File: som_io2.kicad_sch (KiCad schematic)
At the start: 8 parts, among them J1 Hermaphroditic_Molex_203456-0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, Y1 Oscillator_156.25MHz_SG3225EEN

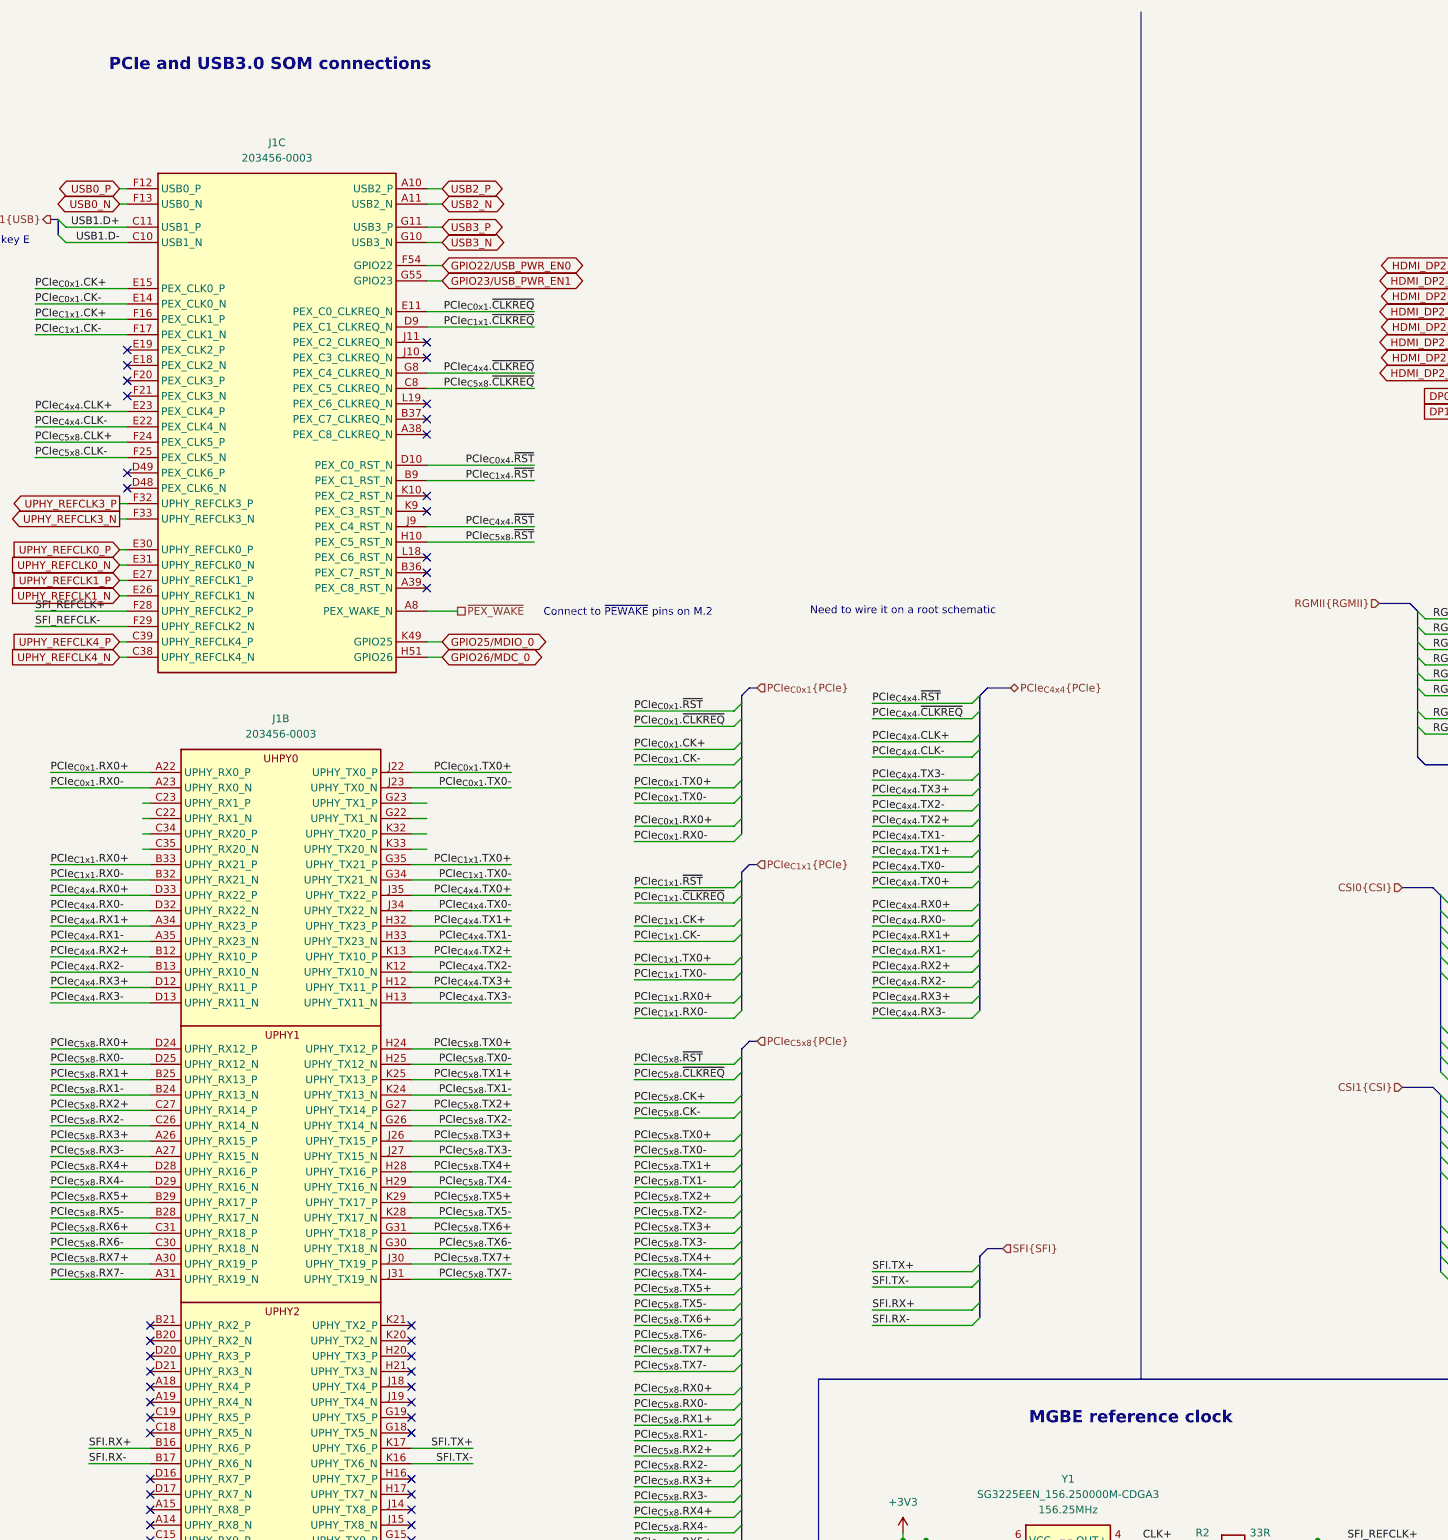
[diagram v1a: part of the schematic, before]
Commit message: [#82837] Standardise sheet sections text size
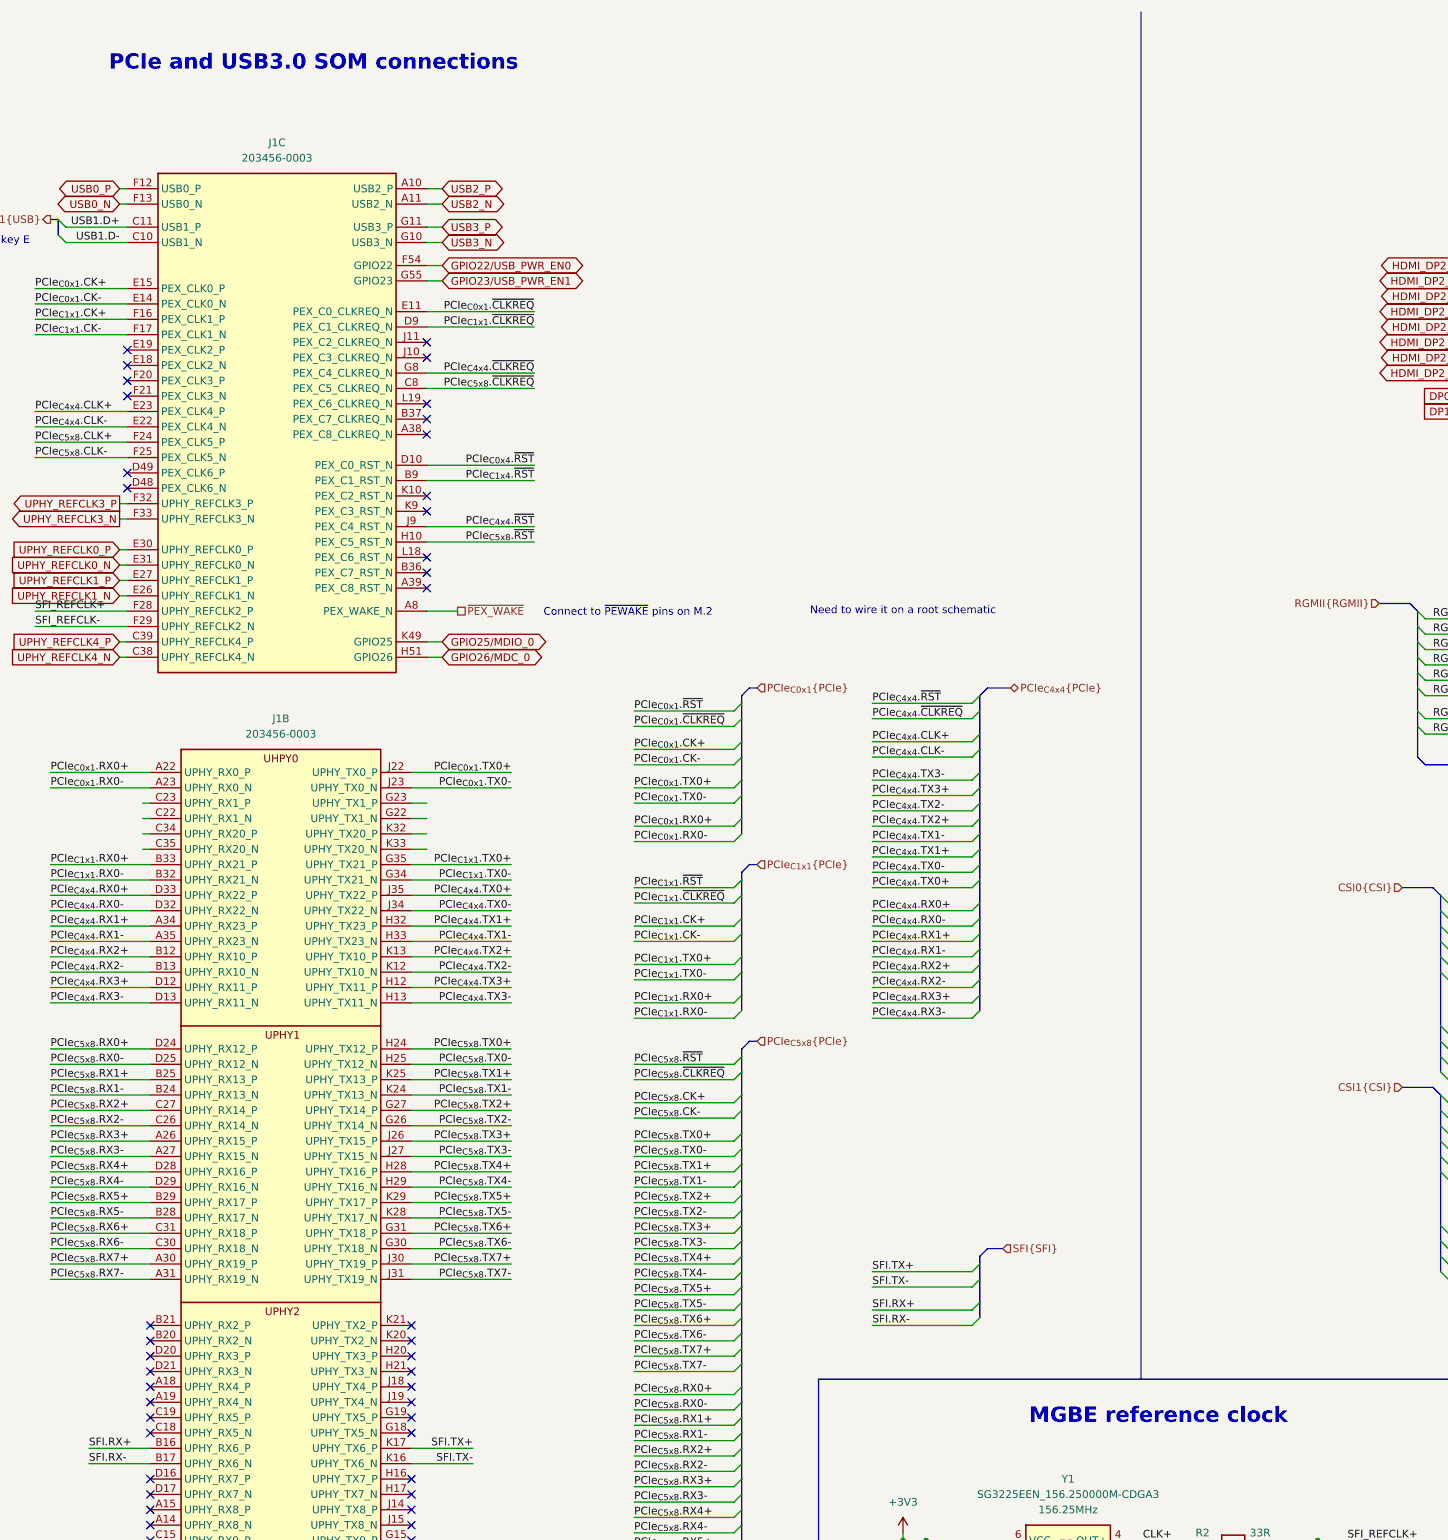
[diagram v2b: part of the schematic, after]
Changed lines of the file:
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@@
 		(effects
 			(font
-				(size 2 2)
+				(size 2.54 2.54)
 				(thickness 0.508)
 				(bold yes)
@@
 		(effects
 			(font
-				(size 2 2)
+				(size 2.54 2.54)
 				(thickness 0.508)
 				(bold yes)

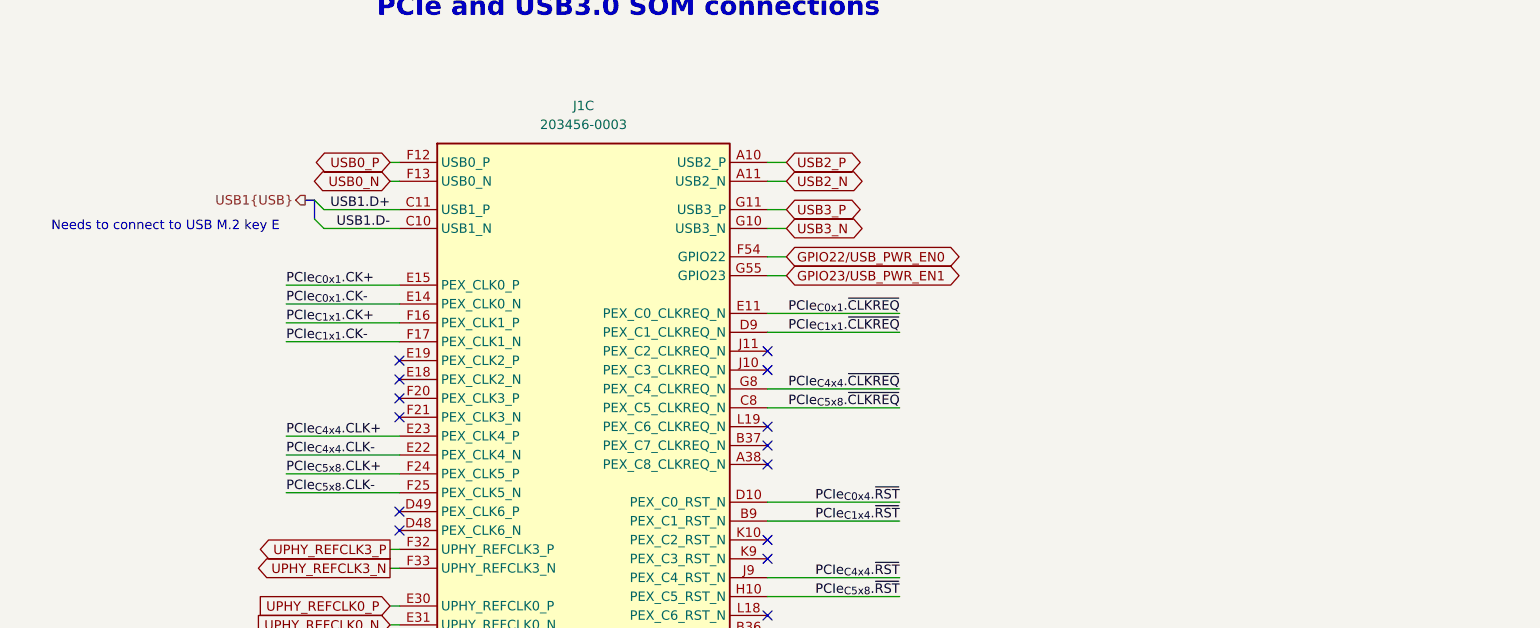
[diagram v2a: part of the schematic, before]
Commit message: [#82837] Reorganize project: split each USB subsheet into two subsheets
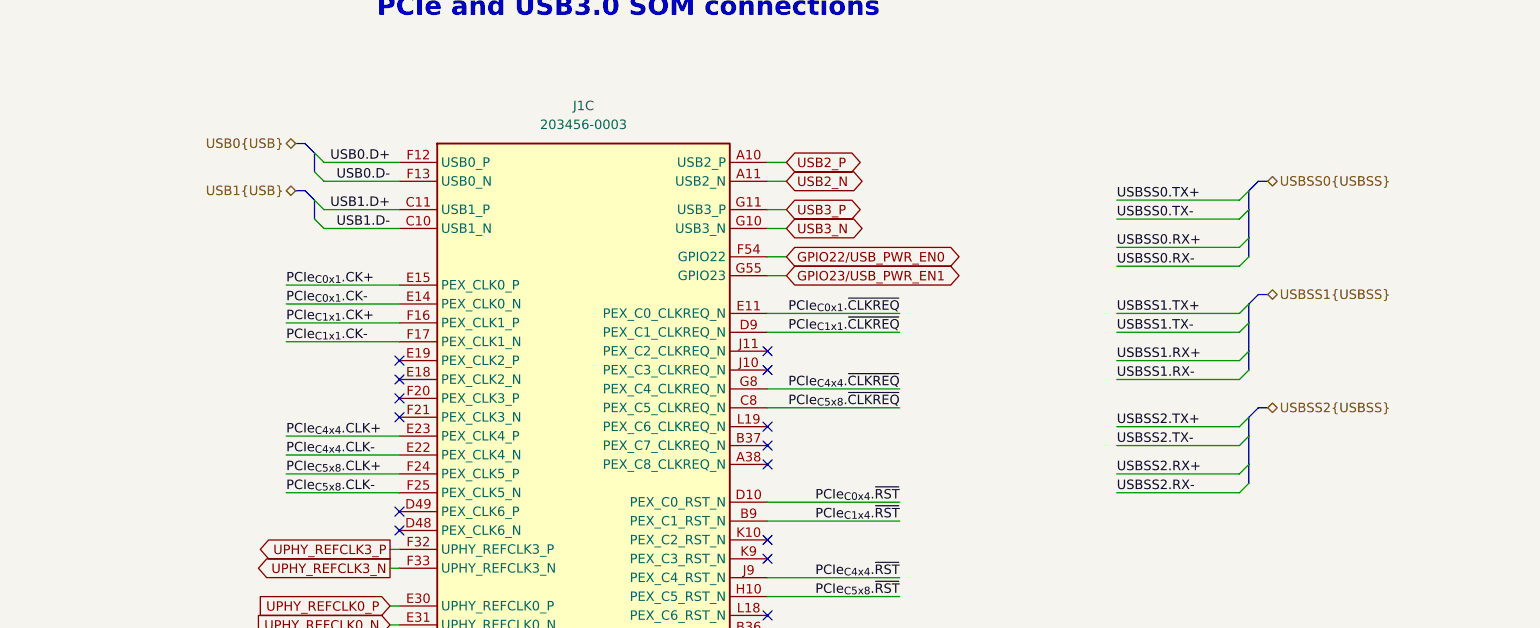
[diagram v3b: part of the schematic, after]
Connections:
- net USB0_N renamed USB0.D-
- net USB0_P renamed USB0.D+
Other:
- note removed: "Needs to connect to USB M.2 key E"

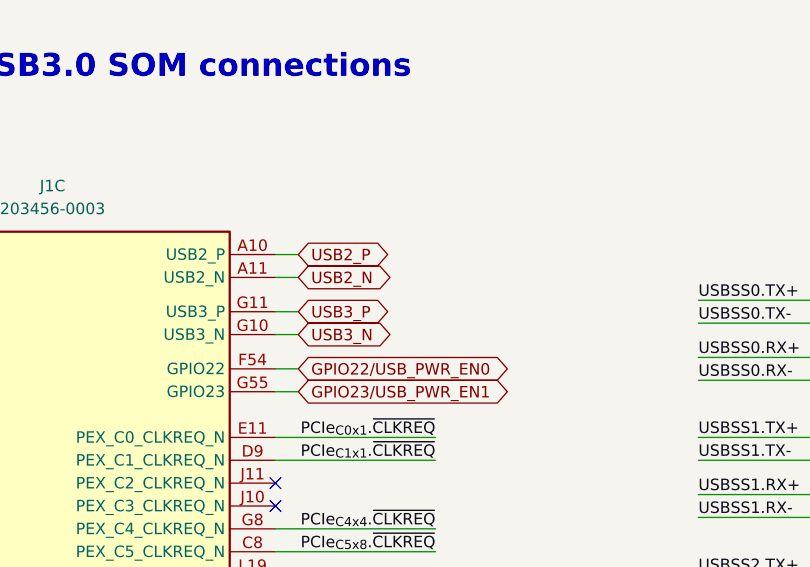
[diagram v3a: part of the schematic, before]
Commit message: [#82837] Cleanup USB Hub schematic and add vbus connections
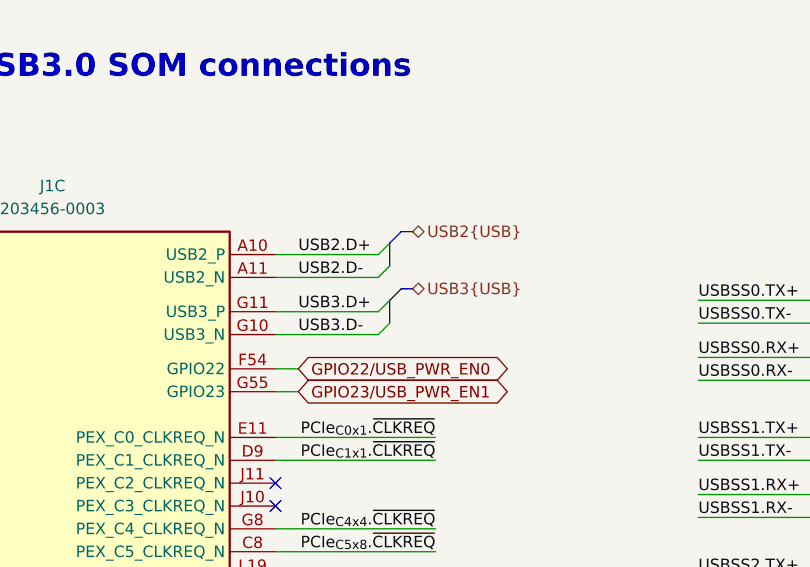
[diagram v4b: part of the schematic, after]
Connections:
- net USB2_N renamed USB2.D-
- net USB2_P renamed USB2.D+
- net USB3_N renamed USB3.D-
- net USB3_P renamed USB3.D+
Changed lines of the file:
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@@
 	)
 	(bus_entry
+		(at 138.43 49.53)
+		(size 1.27 -1.27)
+		(stroke
+			(width 0)
+			(type default)
+		)
+	)
+	(bus_entry
 		(at 179.07 163.83)
 		(size -1.27 1.27)
@@
 	)
 	(bus_entry
+		(at 138.43 43.18)
+		(size 1.27 -1.27)
+		(stroke
+			(width 0)
+			(type default)
+		)
+	)
+	(bus_entry
 		(at 179.07 193.04)
 		(size -1.27 1.27)
@@
 	)
 	(bus_entry
+		(at 138.43 46.99)
+		(size 1.27 -1.27)
+		(stroke
+			(width 0)
+			(type default)
+		)
+	)
+	(bus_entry
 		(at 191.77 83.82)
 		(size -1.27 1.27)
@@
 	)
 	(bus_entry
+		(at 138.43 40.64)
+		(size 1.27 -1.27)
+		(stroke
+			(width 0)
+			(type default)
+		)
+	)
+	(bus_entry
 		(at 179.07 196.85)
 		(size -1.27 1.27)
@@
 	(wire
 		(pts
-			(xy 129.54 40.64) (xy 127 40.64)
+			(xy 127 40.64) (xy 138.43 40.64)
 		)
 		(stroke
@@
 	(wire
 		(pts
-			(xy 129.54 46.99) (xy 127 46.99)
+			(xy 127 46.99) (xy 138.43 46.99)
 		)
 		(stroke
@@
 	(bus
 		(pts
+			(xy 140.97 38.1) (xy 139.7 39.37)
+		)
+		(stroke
+			(width 0)
+			(type default)
+		)
+	)
+	(bus
+		(pts
 			(xy 194.31 73.66) (xy 193.04 73.66)
 		)
@@
 	(bus
 		(pts
+			(xy 139.7 48.26) (xy 139.7 45.72)
+		)
+		(stroke
+			(width 0)
+			(type default)
+		)
+	)
+	(bus
+		(pts
 			(xy 179.07 196.85) (xy 179.07 199.39)
 		)
@@
 	(wire
 		(pts
-			(xy 129.54 49.53) (xy 127 49.53)
+			(xy 127 49.53) (xy 138.43 49.53)
 		)
 		(stroke
@@
 	(bus
 		(pts
+			(xy 142.24 38.1) (xy 140.97 38.1)
+		)
+		(stroke
+			(width 0)
+			(type default)
+		)
+	)
+	(bus
+		(pts
 			(xy 179.07 134.62) (xy 179.07 138.43)
 		)
@@
 		)
 	)
+	(bus
+		(pts
+			(xy 140.97 44.45) (xy 139.7 45.72)
+		)
+		(stroke
+			(width 0)
+			(type default)
+		)
+	)
 	(wire
 		(pts
@@
 	(bus
 		(pts
+			(xy 142.24 44.45) (xy 140.97 44.45)
+		)
+		(stroke
+			(width 0)
+			(type default)
+		)
+	)
+	(bus
+		(pts
 			(xy 361.95 179.07) (xy 361.95 181.61)
 		)
@@
 	(bus
 		(pts
+			(xy 139.7 41.91) (xy 139.7 39.37)
+		)
+		(stroke
+			(width 0)
+			(type default)
+		)
+	)
+	(bus
+		(pts
 			(xy 179.07 246.38) (xy 179.07 248.92)
 		)
@@
 	(wire
 		(pts
-			(xy 129.54 43.18) (xy 127 43.18)
+			(xy 127 43.18) (xy 138.43 43.18)
 		)
 		(stroke
@@
 		)
 	)
+	(label "USB2.D-"
+		(at 129.54 43.18 0)
+		(effects
+			(font
+				(size 1.27 1.27)
+			)
+			(justify left bottom)
+		)
+	)
 	(label "PCIe_{C5x8}.RX1+"
 		(at 64.77 187.96 0)
@@
 		)
 	)
+	(label "USB3.D+"
+		(at 129.54 46.99 0)
+		(effects
+			(font
+				(size 1.27 1.27)
+			)
+			(justify left bottom)
+		)
+	)
 	(label "CSI0.CLK+"
 		(at 295.91 158.75 0)
@@
 		)
 	)
+	(label "USB2.D+"
+		(at 129.54 40.64 0)
+		(effects
+			(font
+				(size 1.27 1.27)
+			)
+			(justify left bottom)
+		)
+	)
 	(label "USB1.D+"
 		(at 76.2 46.99 180)
@@
 		)
 	)
+	(label "USB3.D-"
+		(at 129.54 49.53 0)
+		(effects
+			(font
+				(size 1.27 1.27)
+			)
+			(justify left bottom)
+		)
+	)
 	(label "USB0.D+"
 		(at 76.2 40.64 180)
@@
 		)
 	)
-	(global_label "USB3_P"
-		(shape bidirectional)
-		(at 129.54 46.99 0)
-		(fields_autoplaced yes)
-		(effects
-			(font
-				(size 1.27 1.27)
-			)
-			(justify left)
-		)
-		(property "Intersheetrefs" "${INTERSHEET_REFS}"
-			(at 140.8936 46.99 0)
-			(effects
-				(font
-					(size 1.27 1.27)
-				)
-				(justify left)
-				(hide yes)
-			)
-		)
-	)
 	(global_label "UPHY_REFCLK1_N"
 		(shape input)
@@
 		)
 	)
-	(global_label "USB2_N"
-		(shape bidirectional)
-		(at 129.54 43.18 0)
-		(fields_autoplaced yes)
-		(effects
-			(font
-				(size 1.27 1.27)
-			)
-			(justify left)
-		)
-		(property "Intersheetrefs" "${INTERSHEET_REFS}"
-			(at 140.9541 43.18 0)
-			(effects
-				(font
-					(size 1.27 1.27)
-				)
-				(justify left)
-				(hide yes)
-			)
-		)
-	)
 	(global_label "DP2_AUX_CH_P"
 		(shape bidirectional)
@@
 		)
 	)
-	(global_label "USB2_P"
-		(shape bidirectional)
-		(at 129.54 40.64 0)
-		(fields_autoplaced yes)
-		(effects
-			(font
-				(size 1.27 1.27)
-			)
-			(justify left)
-		)
-		(property "Intersheetrefs" "${INTERSHEET_REFS}"
-			(at 140.8936 40.64 0)
-			(effects
-				(font
-					(size 1.27 1.27)
-				)
-				(justify left)
-				(hide yes)
-			)
-		)
-	)
 	(global_label "UPHY_REFCLK1_P"
 		(shape input)
@@
 		)
 	)
-	(global_label "USB3_N"
-		(shape bidirectional)
-		(at 129.54 49.53 0)
-		(fields_autoplaced yes)
-		(effects
-			(font
-				(size 1.27 1.27)
-			)
-			(justify left)
-		)
-		(property "Intersheetrefs" "${INTERSHEET_REFS}"
-			(at 140.9541 49.53 0)
-			(effects
-				(font
-					(size 1.27 1.27)
-				)
-				(justify left)
-				(hide yes)
-			)
-		)
-	)
 	(global_label "UPHY_REFCLK0_P"
 		(shape input)
@@
 		)
 	)
+	(hierarchical_label "USB2{USB}"
+		(shape bidirectional)
+		(at 142.24 38.1 0)
+		(effects
+			(font
+				(size 1.27 1.27)
+			)
+			(justify left)
+		)
+	)
 	(hierarchical_label "USB1{USB}"
 		(shape bidirectional)
@@
 		(effects
 			(font
+				(size 1.27 1.27)
+			)
+			(justify left)
+		)
+	)
+	(hierarchical_label "USB3{USB}"
+		(shape bidirectional)
+		(at 142.24 44.45 0)
+		(effects
+			(font
